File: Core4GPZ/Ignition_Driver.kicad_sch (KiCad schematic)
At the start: 14 parts, among them Q1 Q_NIGBT_CEG, Q2 Q_PNP_EBC, Q3 Q_PNP_EBC, Q4 Q_NIGBT_CEG

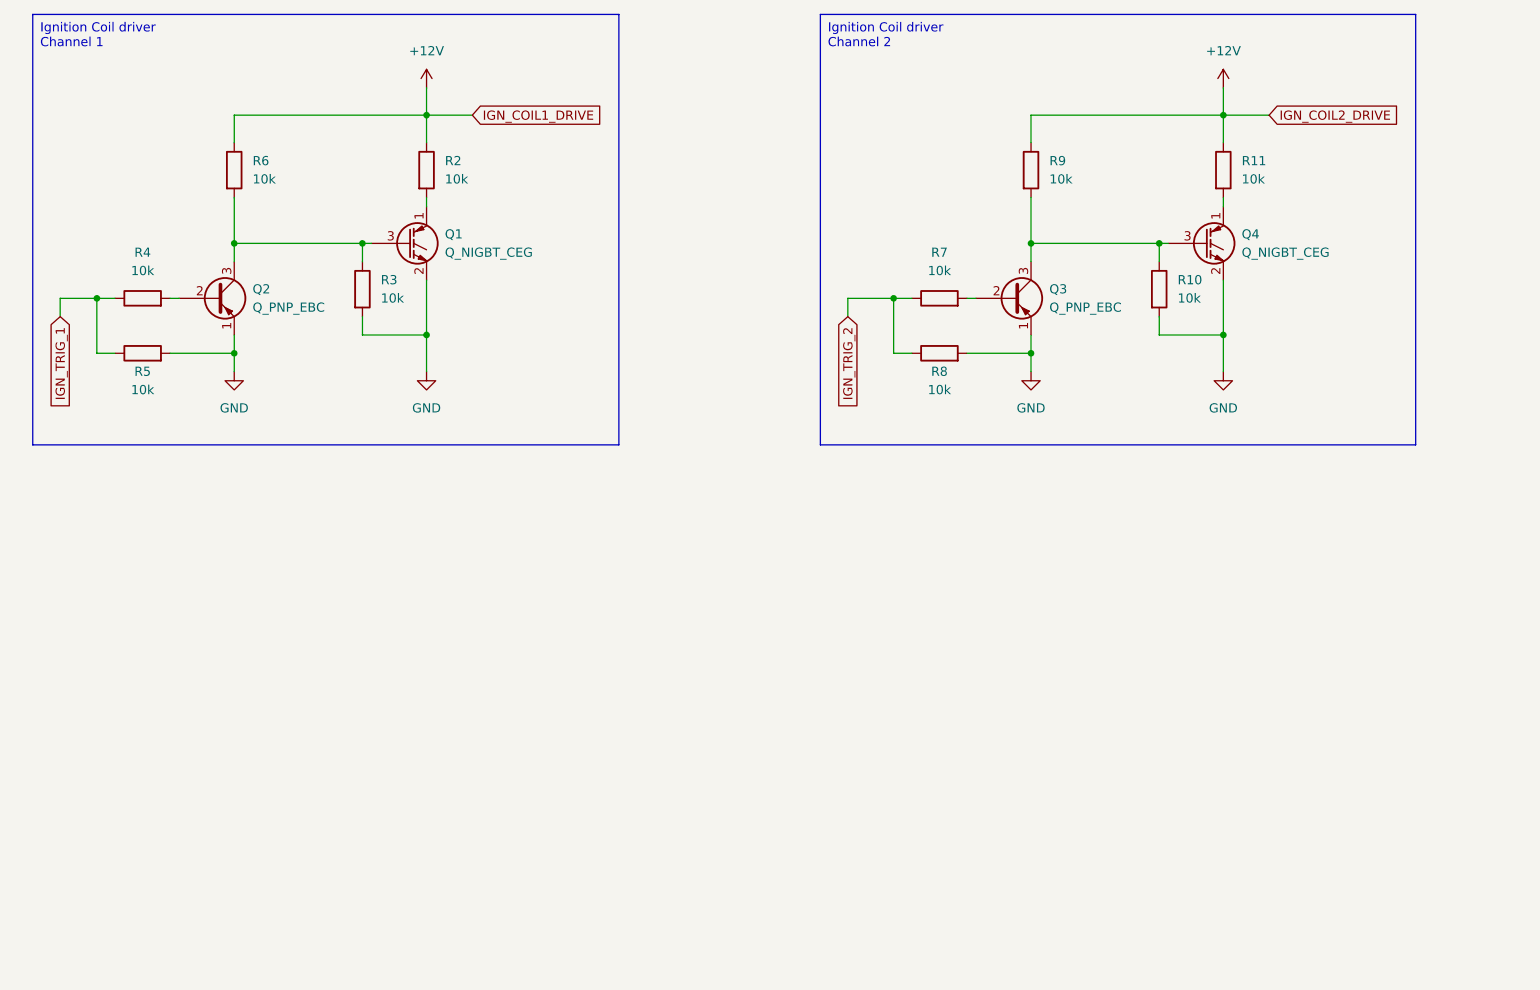
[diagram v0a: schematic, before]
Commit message: Updated security wiring and changed IGN driver for MOSFET
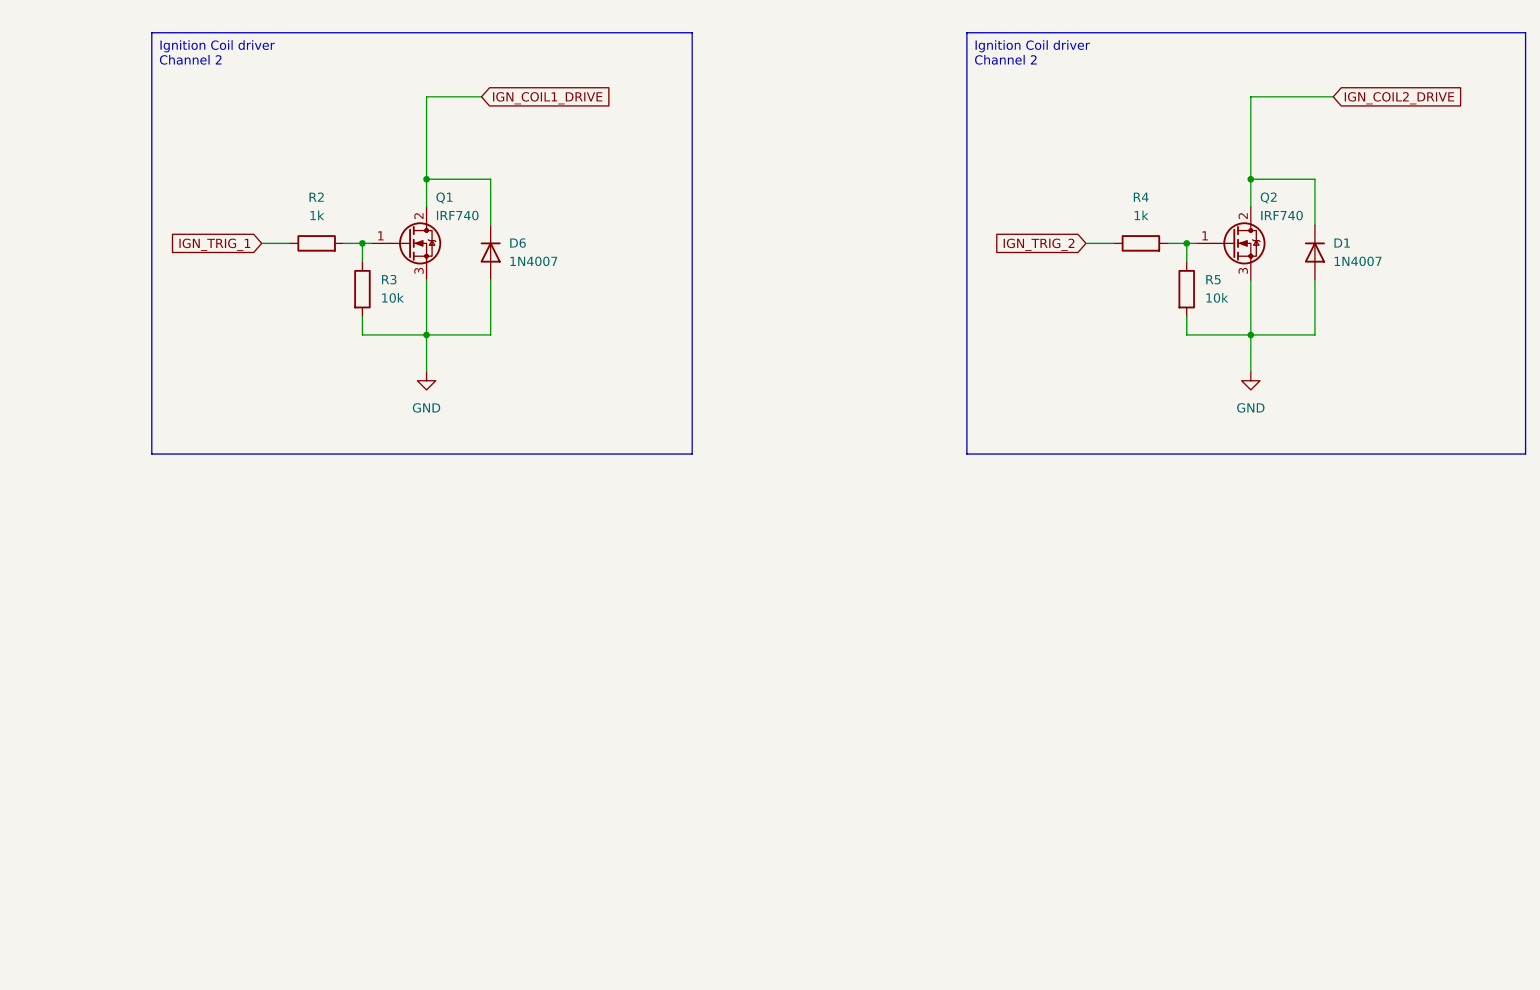
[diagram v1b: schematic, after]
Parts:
- removed Q1, Q4: Q_NIGBT_CEG, Package_TO_SOT_THT:TO-247-3_Vertical, symbol Device:Q_NIGBT_CEG
- removed Q2, Q3: Q_PNP_EBC, Package_TO_SOT_THT:TO-92L_Inline, symbol Device:Q_PNP_EBC
- removed R10, R11, R6, R7, R8, R9: 10k, Resistor_THT:R_Axial_DIN0207_L6.3mm_D2.5mm_P10.16mm_Horizontal, symbol Device:R
- added D1, D6: 1N4007, Diode_THT:D_A-405_P2.54mm_Vertical_AnodeUp, symbol Device:D
- added Q1, Q2: IRF740, Package_TO_SOT_THT:TO-220-3_Horizontal_TabDown, symbol Transistor_FET:IRF740
- R2, R4: value 10k -> 1k
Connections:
- net +12V is gone; now on net IGN_TRIG_1: R2.1
- net GND: now also D1.2 (A), D6.2 (A), Q1.3 (S), Q2.3 (S)
- net IGN_TRIG_1: no longer R4.1, R5.1
- net IGN_TRIG_2: now also R4.1
- net at R2.2: now also R3.1, Q1.1 (G)
- net at R4.2: now also R5.1, Q2.1 (G)
- new net IGN_COIL1_DRIVE: D6.1 (K), Q1.2 (D)
- new net IGN_COIL2_DRIVE: D1.1 (K), Q2.2 (D)

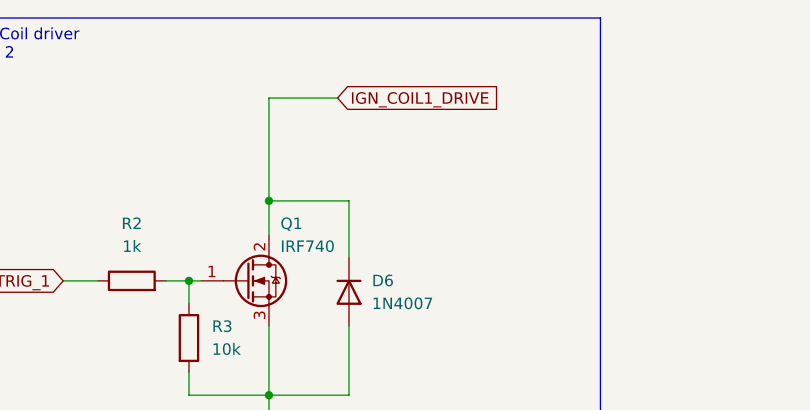
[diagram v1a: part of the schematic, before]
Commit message: Changed Connectors for Molex CMC 48pins Black.
Changed ECU Connector for Molex CMC 48pins Black, for compacity and cost reduction. Designed custom Footprint for this purpose
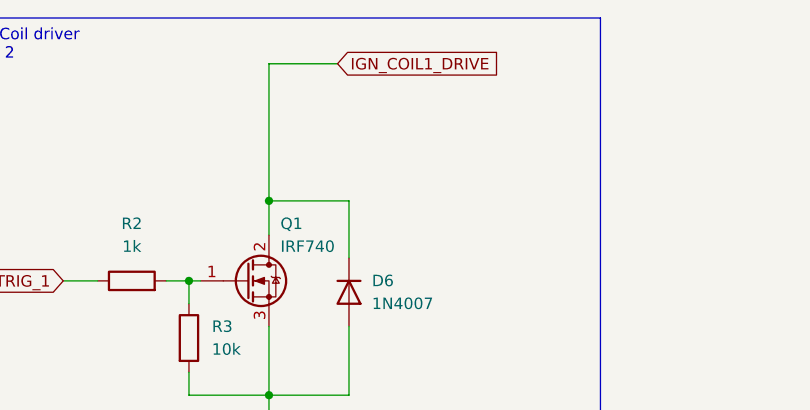
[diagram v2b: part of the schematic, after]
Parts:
- Q1, Q2: footprint Package_TO_SOT_THT:TO-220-3_Horizontal_TabDown -> Package_TO_SOT_THT:TO-220-3_Vertical
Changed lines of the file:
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@@
     (stroke (width 0) (type default))
   )
-  (wire (pts (xy 102.87 34.29) (xy 110.49 34.29))
+  (wire (pts (xy 102.87 30.48) (xy 110.49 30.48))
     (stroke (width 0) (type default))
   )
@@
     (stroke (width 0) (type default))
   )
-  (wire (pts (xy 102.87 34.29) (xy 102.87 45.72))
+  (wire (pts (xy 102.87 30.48) (xy 102.87 45.72))
     (stroke (width 0) (type default))
   )
@@
     )
   )
-  (global_label "IGN_COIL1_DRIVE" (shape input) (at 110.49 34.29 0) (fields_autoplaced)
+  (global_label "IGN_COIL1_DRIVE" (shape input) (at 110.49 30.48 0) (fields_autoplaced)
     (effects (font (size 1.27 1.27)) (justify left))
-    (property "Intersheetrefs" "${INTERSHEET_REFS}" (at 129.441 34.29 0)
+    (property "Intersheetrefs" "${INTERSHEET_REFS}" (at 129.441 30.48 0)
       (effects (font (size 1.27 1.27)) (justify left) hide)
     )
@@
       (effects (font (size 1.27 1.27)) (justify left))
     )
-    (property "Footprint" "Package_TO_SOT_THT:TO-220-3_Horizontal_TabDown" (at 220.98 56.515 0)
+    (property "Footprint" "Package_TO_SOT_THT:TO-220-3_Vertical" (at 220.98 56.515 0)
       (effects (font (size 1.27 1.27) italic) (justify left) hide)
     )
     (property "Datasheet" "http://www.vishay.com/docs/91054/91054.pdf" (at 214.63 54.61 0)
       (effects (font (size 1.27 1.27)) (justify left) hide)
+    )
+    (property "Sim.Device" "NMOS" (at 214.63 54.61 0)
+      (effects (font (size 1.27 1.27)) hide)
+    )
+    (property "Sim.Type" "VDMOS" (at 214.63 54.61 0)
+      (effects (font (size 1.27 1.27)) hide)
+    )
+    (property "Sim.Pins" "1=D 2=G 3=S" (at 214.63 54.61 0)
+      (effects (font (size 1.27 1.27)) hide)
     )
     (pin "3")
@@
       (effects (font (size 1.27 1.27)) (justify left))
     )
-    (property "Footprint" "Package_TO_SOT_THT:TO-220-3_Horizontal_TabDown" (at 106.68 56.515 0)
+    (property "Footprint" "Package_TO_SOT_THT:TO-220-3_Vertical" (at 106.68 56.515 0)
       (effects (font (size 1.27 1.27) italic) (justify left) hide)
     )

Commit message: Test montage générateur de Haute tension
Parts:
- added D5, D7: 1N4007, Diode_SMD:D_1206_3216Metric_Pad1.42x1.75mm_HandSolder, symbol Device:D
- added Q3, Q4: IRF740, Package_TO_SOT_THT:TO-220-3_Vertical, symbol Transistor_FET:IRF740
- added R1, R7, R8, R9: 1k, Resistor_SMD:R_0805_2012Metric_Pad1.20x1.40mm_HandSolder, symbol Device:R
- D1, D6: footprint Diode_THT:D_A-405_P2.54mm_Vertical_AnodeUp -> Diode_SMD:D_1206_3216Metric_Pad1.42x1.75mm_HandSolder
- R2, R4: footprint Resistor_THT:R_Axial_DIN0207_L6.3mm_D2.5mm_P10.16mm_Horizontal -> Resistor_SMD:R_0805_2012Metric_Pad1.20x1.40mm_HandSolder
- R3, R5: value 10k -> 1k; footprint Resistor_THT:R_Axial_DIN0207_L6.3mm_D2.5mm_P10.16mm_Horizontal -> Resistor_SMD:R_0805_2012Metric_Pad1.20x1.40mm_HandSolder
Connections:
- net GND: now also R2.1, R4.1, D5.2 (A), D7.2 (A), Q3.3 (S), Q4.3 (S), R7.1, R9.1; no longer R3.2, R5.2
- net IGN_TRIG_1: now also R1.2; no longer R2.1
- net IGN_TRIG_2: now also R3.2; no longer R4.1
- net at Q2.1 (G), R4.2: now also R3.1; no longer R5.1
- net at Q1.1 (G), R2.2: now also R1.1; no longer R3.1
- new net: Q3.1 (G), R5.1, R7.2
- new net: Q4.1 (G), R8.1, R9.2
- new net IGN_COIL3_DRIVE: D5.1 (K), Q3.2 (D)
- new net IGN_COIL4_DRIVE: D7.1 (K), Q4.2 (D)
- new net IGN_TRIG_3: R5.2
- new net IGN_TRIG_4: R8.2
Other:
- moved on the sheet: D6, Q1, Q2, R2

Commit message: Updated to Kicad 8.0
Also added Highvoltage circuit
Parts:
- removed Q1, Q2, Q3, Q4: IRF740, Package_TO_SOT_THT:TO-220-3_Vertical, symbol Transistor_FET:IRF740
- added Q1, Q2, Q3, Q4: IRF3205, Package_TO_SOT_THT:TO-220-3_Vertical, symbol Transistor_FET:IRF3205
- R2, R4, R7, R9: value 1k -> 10k
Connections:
- net GND: now also Q1.3 (S), Q2.3 (S), Q3.3 (S), Q4.3 (S)
- net IGN_COIL1_DRIVE: now also Q1.2 (D)
- net IGN_COIL2_DRIVE: now also Q2.2 (D)
- net IGN_COIL3_DRIVE: now also Q3.2 (D)
- net IGN_COIL4_DRIVE: now also Q4.2 (D)
- net at R3.1, R4.2: now also Q2.1 (G)
- net at R1.1, R2.2: now also Q1.1 (G)
- net at R5.1, R7.2: now also Q3.1 (G)
- net at R8.1, R9.2: now also Q4.1 (G)

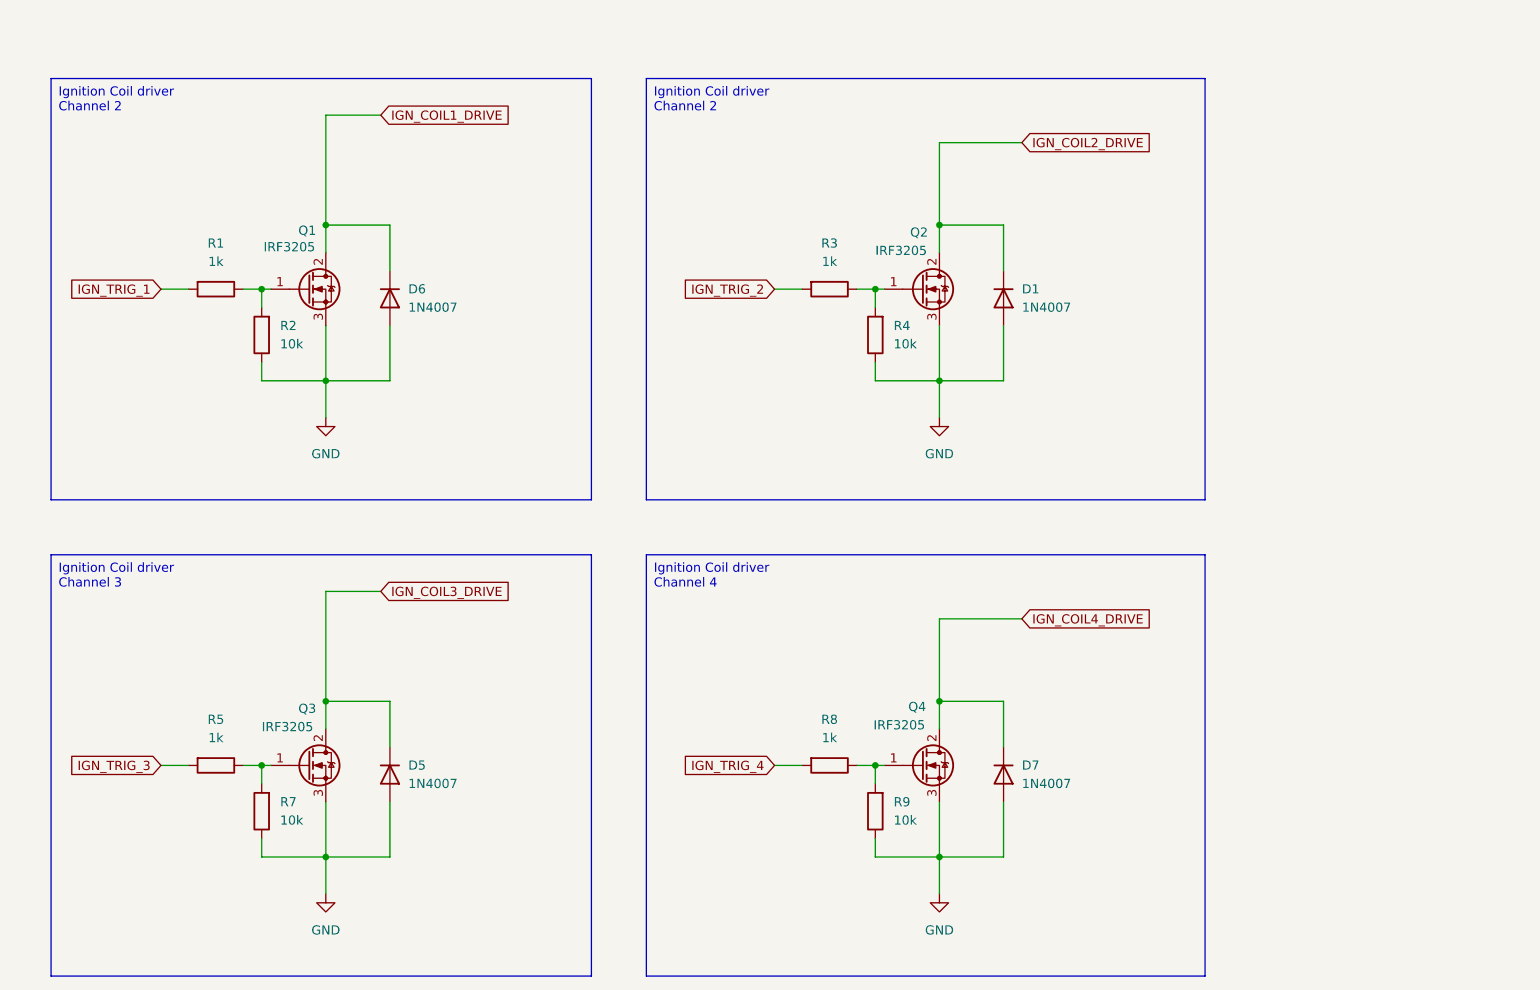
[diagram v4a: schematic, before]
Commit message: Added VR Conditionner for Cam/Crank SNSR
Added some jumper for prototyping and testing purposes
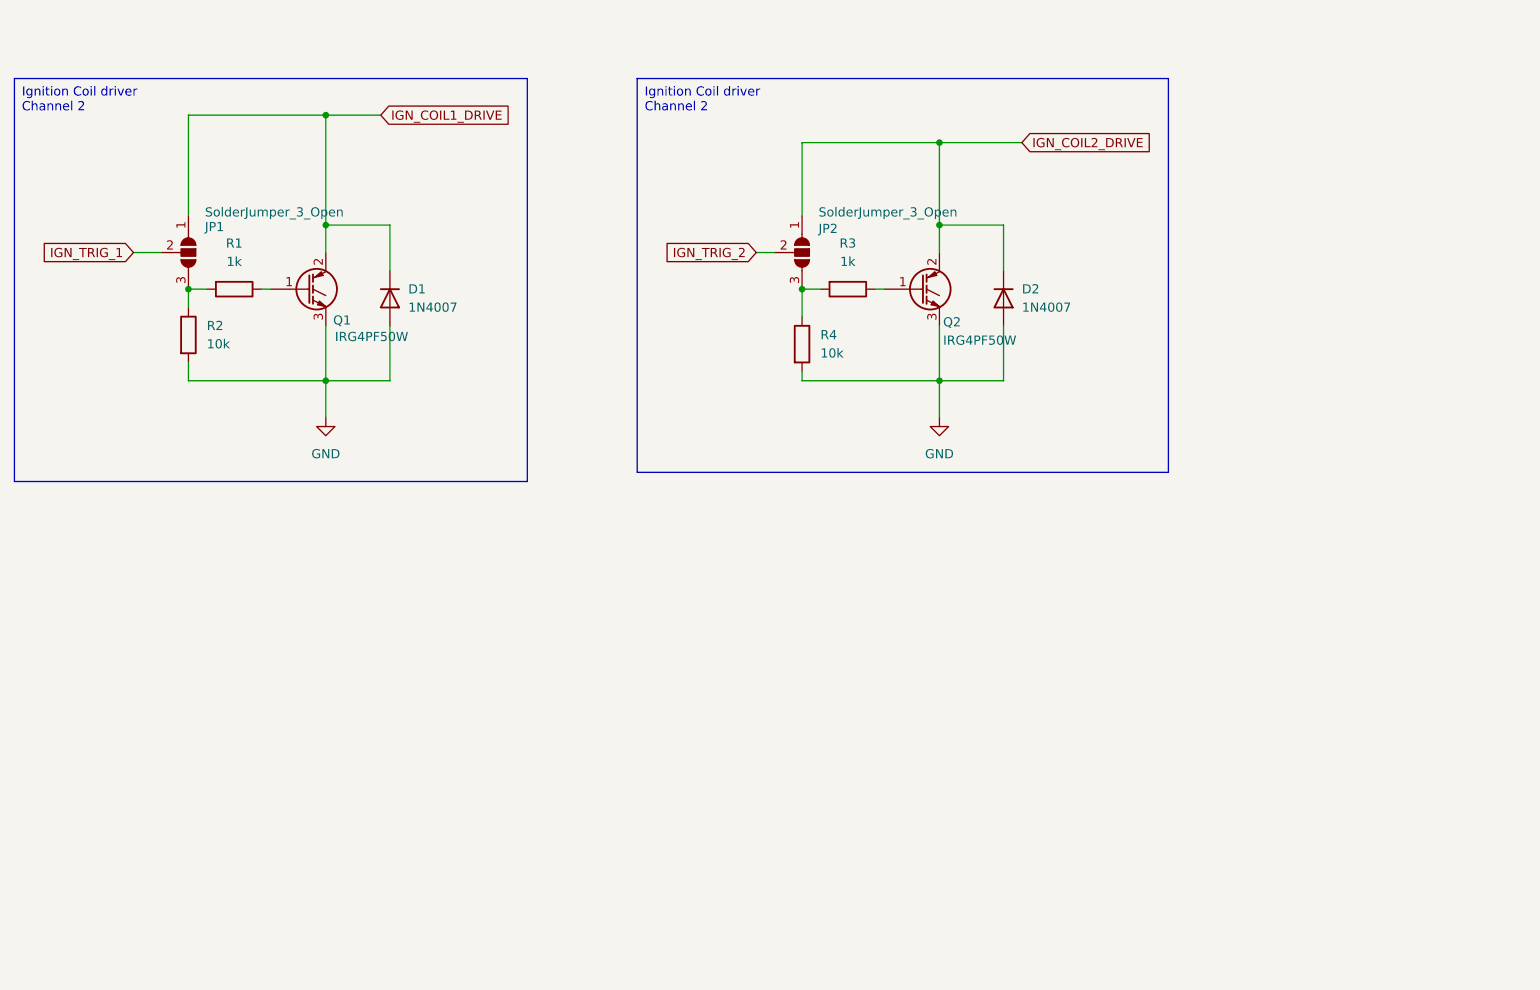
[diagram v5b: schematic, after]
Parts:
- removed D1, D5, D7: 1N4007, Diode_SMD:D_1206_3216Metric_Pad1.42x1.75mm_HandSolder, symbol Device:D
- removed Q1, Q2, Q3, Q4: IRF3205, Package_TO_SOT_THT:TO-220-3_Vertical, symbol Transistor_FET:IRF3205
- removed R5, R8: 1k, Resistor_SMD:R_0805_2012Metric_Pad1.20x1.40mm_HandSolder, symbol Device:R
- removed R7, R9: 10k, Resistor_SMD:R_0805_2012Metric_Pad1.20x1.40mm_HandSolder, symbol Device:R
- added D2: 1N4007, Diode_THT:D_DO-41_SOD81_P2.54mm_Vertical_KathodeUp, symbol Device:D
- added JP1, JP2: SolderJumper_3_Open, symbol Jumper:SolderJumper_3_Open
- added Q1, Q2: IRG4PF50W, Package_TO_SOT_THT:TO-247-3_Vertical, symbol Transistor_IGBT:IRG4PF50W
- D1: renamed from D6; footprint Diode_SMD:D_1206_3216Metric_Pad1.42x1.75mm_HandSolder -> Diode_THT:D_DO-41_SOD81_P2.54mm_Vertical_KathodeUp
- R1, R2, R3, R4: footprint Resistor_SMD:R_0805_2012Metric_Pad1.20x1.40mm_HandSolder -> Resistor_THT:R_Axial_DIN0204_L3.6mm_D1.6mm_P5.08mm_Horizontal
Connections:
- net GND: now also R2.2, R4.2, D2.2 (A), Q1.3 (E), Q2.3 (E); no longer R2.1, R4.1
- net IGN_COIL1_DRIVE: now also JP1.1 (A), Q1.2 (C)
- net IGN_COIL2_DRIVE: now also D2.1 (K), JP2.1 (A), Q2.2 (C)
- net IGN_TRIG_1: now also JP1.2 (C); no longer R1.2
- net IGN_TRIG_2: now also JP2.2 (C); no longer R3.2
- net at R3.1: now also Q2.1 (G); no longer R4.2
- net at R1.1: now also Q1.1 (G); no longer R2.2
- new net: JP1.3 (B), R1.2, R2.1
- new net: JP2.3 (B), R3.2, R4.1
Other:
- moved on the sheet: R1
